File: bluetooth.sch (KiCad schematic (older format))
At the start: 53 parts, among them P100 CONN_2, P110 CONN_1, P111 CONN_1, P112 CONN_1, P113 CONN_1, P114 CONN_1, P115 CONN_1, P130 CONN_1, P131 CONN_1, Q1 MOSFET_N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

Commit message: Fix capacitor values for NCP1402
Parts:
- C12: value 10u -> 68u
- C15: value 68u -> 10u
- U3: value NCP1402 -> NCP1402SN50
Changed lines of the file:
@@
 P 2700 4900
 F 0 "U3" H 2700 4700 60  0000 C CNN
-F 1 "NCP1402" H 2700 5100 60  0000 C CNN
+F 1 "NCP1402SN50" H 2700 5100 60  0000 C CNN
 F 2 "" H 2700 4900 60  0000 C CNN
 F 3 "" H 2700 4900 60  0000 C CNN
@@
 P 4350 4850
 F 0 "C15" H 4400 4950 40  0000 L CNN
-F 1 "68u" H 4400 4750 40  0000 L CNN
+F 1 "10u" H 4400 4750 40  0000 L CNN
 F 2 "" H 4450 4700 30  0000 C CNN
 F 3 "" H 4350 4850 300 0000 C CNN
@@
 P 1600 4850
 F 0 "C12" H 1650 4950 40  0000 L CNN
-F 1 "10u" H 1650 4750 40  0000 L CNN
+F 1 "68u" H 1650 4750 40  0000 L CNN
 F 2 "" H 1700 4700 30  0000 C CNN
 F 3 "" H 1600 4850 300 0000 C CNN

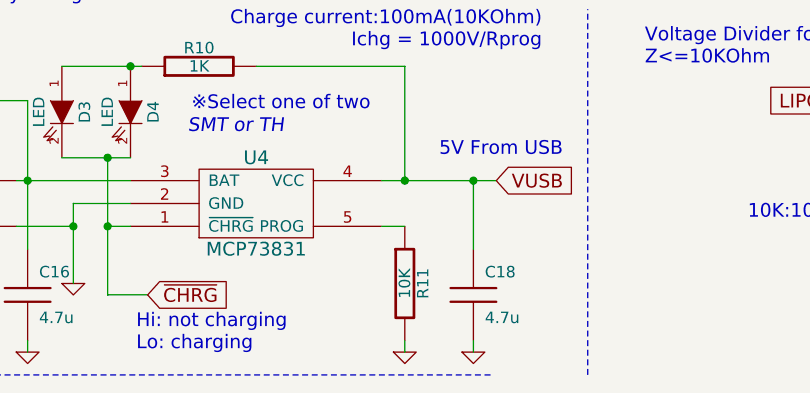
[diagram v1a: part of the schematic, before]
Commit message: Change value 10K to Rprog for charger resistor
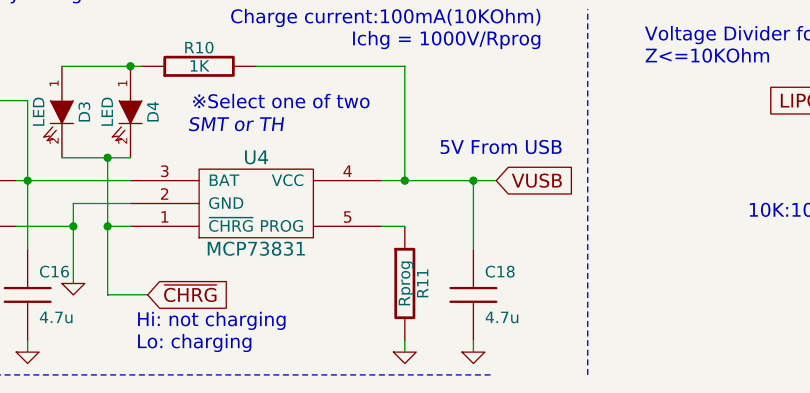
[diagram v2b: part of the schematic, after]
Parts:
- R11: value 10K -> Rprog
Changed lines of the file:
@@
 P 6200 7150
 F 0 "R11" V 6280 7150 50  0000 C CNN
-F 1 "10K" V 6200 7150 50  0000 C CNN
+F 1 "Rprog" V 6200 7150 50  0000 C CNN
 F 2 "" H 6200 7150 60  0000 C CNN
 F 3 "" H 6200 7150 60  0000 C CNN

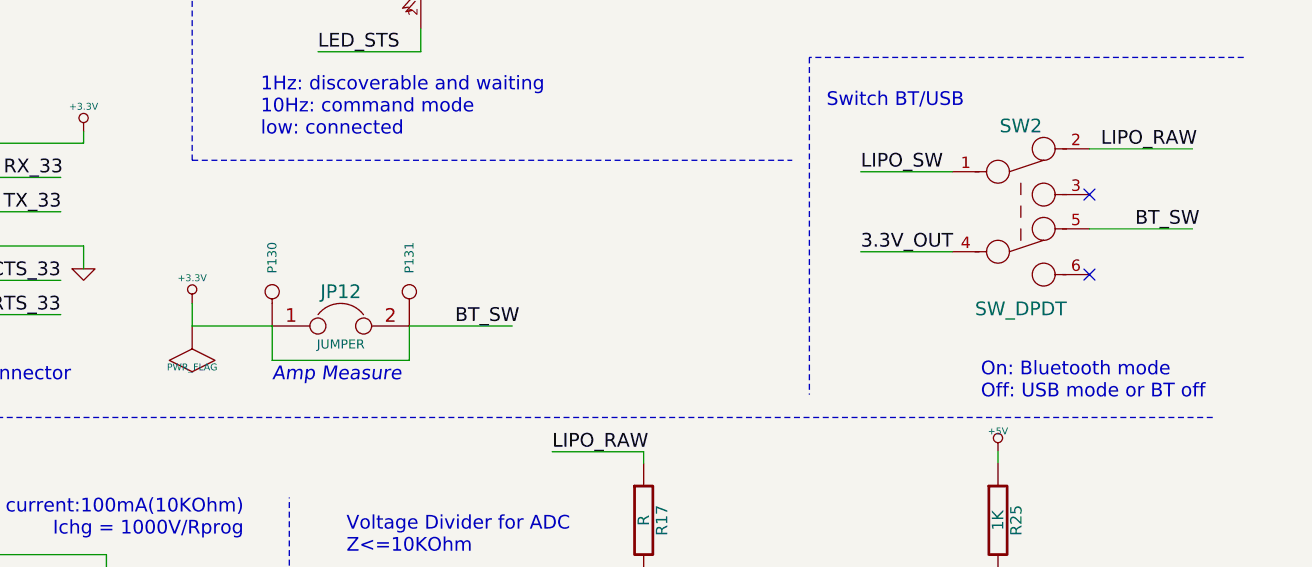
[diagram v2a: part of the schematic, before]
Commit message: Remove jumpers of 5V, 3.3V and HHKB amp measure
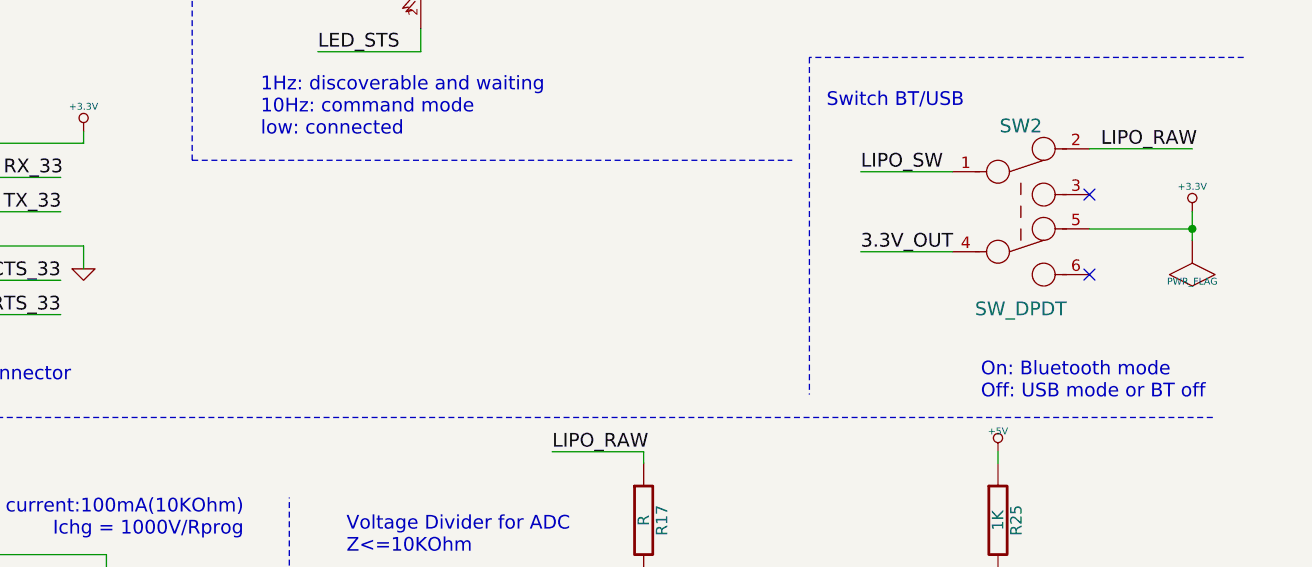
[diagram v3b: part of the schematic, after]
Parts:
- removed JP12: JUMPER, symbol JUMPER
- removed P130, P131: CONN_1, symbol CONN_1
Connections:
- net labels removed: BT_SW
- wire segments 142 -> 137
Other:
- note removed: "Amp Measure"
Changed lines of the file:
@@
 JST PH2
 $Comp
-L GND #PWR030
+L GND #PWR028
 U 1 1 51AFD4B7
 P 4750 7150
-F 0 "#PWR030" H 4750 7150 30  0001 C CNN
+F 0 "#PWR028" H 4750 7150 30  0001 C CNN
 F 1 "GND" H 4750 7080 30  0001 C CNN
 F 2 "" H 4750 7150 60  0000 C CNN
@@
 PSEL
 $Comp
-L GND #PWR031
+L GND #PWR029
 U 1 1 51B36189
 P 1600 5150
-F 0 "#PWR031" H 1600 5150 30  0001 C CNN
+F 0 "#PWR029" H 1600 5150 30  0001 C CNN
 F 1 "GND" H 1600 5080 30  0001 C CNN
 F 2 "" H 1600 5150 60  0000 C CNN
@@
 $EndComp
 $Comp
-L GND #PWR032
+L GND #PWR030
 U 1 1 51B36198
 P 4350 5150
-F 0 "#PWR032" H 4350 5150 30  0001 C CNN
+F 0 "#PWR030" H 4350 5150 30  0001 C CNN
 F 1 "GND" H 4350 5080 30  0001 C CNN
 F 2 "" H 4350 5150 60  0000 C CNN
@@
 $EndComp
 $Comp
-L GND #PWR033
+L GND #PWR031
 U 1 1 51B36208
 P 3400 5150
-F 0 "#PWR033" H 3400 5150 30  0001 C CNN
+F 0 "#PWR031" H 3400 5150 30  0001 C CNN
 F 1 "GND" H 3400 5080 30  0001 C CNN
 F 2 "" H 3400 5150 60  0000 C CNN
@@
 $EndComp
 $Comp
-L GND #PWR034
+L GND #PWR032
 U 1 1 51B4212D
 P 1250 3150
-F 0 "#PWR034" H 1250 3150 30  0001 C CNN
+F 0 "#PWR032" H 1250 3150 30  0001 C CNN
 F 1 "GND" H 1250 3080 30  0001 C CNN
 F 2 "" H 1250 3150 60  0000 C CNN
@@
 $EndComp
 $Comp
-L GND #PWR035
+L GND #PWR033
 U 1 1 51B4213C
 P 3300 3150
-F 0 "#PWR035" H 3300 3150 30  0001 C CNN
+F 0 "#PWR033" H 3300 3150 30  0001 C CNN
 F 1 "GND" H 3300 3080 30  0001 C CNN
 F 2 "" H 3300 3150 60  0000 C CNN
@@
 $EndComp
 $Comp
-L GND #PWR036
+L GND #PWR034
 U 1 1 51B421C0
 P 1650 3150
-F 0 "#PWR036" H 1650 3150 30  0001 C CNN
+F 0 "#PWR034" H 1650 3150 30  0001 C CNN
 F 1 "GND" H 1650 3080 30  0001 C CNN
 F 2 "" H 1650 3150 60  0000 C CNN
@@
 $EndComp
 $Comp
-L GND #PWR037
+L GND #PWR035
 U 1 1 51B42259
 P 3000 3350
-F 0 "#PWR037" H 3000 3350 30  0001 C CNN
+F 0 "#PWR035" H 3000 3350 30  0001 C CNN
 F 1 "GND" H 3000 3280 30  0001 C CNN
 F 2 "" H 3000 3350 60  0000 C CNN
@@
 $EndComp
 $Comp
-L GND #PWR038
+L GND #PWR036
 U 1 1 51B4294A
 P 4650 2050
-F 0 "#PWR038" H 4650 2050 30  0001 C CNN
+F 0 "#PWR036" H 4650 2050 30  0001 C CNN
 F 1 "GND" H 4650 1980 30  0001 C CNN
 F 2 "" H 4650 2050 60  0000 C CNN
@@
 $EndComp
 $Comp
-L +5V #PWR039
+L +5V #PWR037
 U 1 1 51B42AA7
 P 1850 1025
-F 0 "#PWR039" H 1850 1115 20  0001 C CNN
+F 0 "#PWR037" H 1850 1115 20  0001 C CNN
 F 1 "+5V" H 1850 1115 30  0000 C CNN
 F 2 "" H 1850 1025 60  0000 C CNN
@@
 $EndComp
 $Comp
-L +3.3V #PWR040
+L +3.3V #PWR038
 U 1 1 51B42AB6
 P 950 1025
-F 0 "#PWR040" H 950 985 30  0001 C CNN
+F 0 "#PWR038" H 950 985 30  0001 C CNN
 F 1 "+3.3V" H 950 1135 30  0000 C CNN
 F 2 "" H 950 1025 60  0000 C CNN
@@
 $EndComp
 $Comp
-L GND #PWR041
+L GND #PWR039
 U 1 1 51B44001
 P 6200 7450
-F 0 "#PWR041" H 6200 7450 30  0001 C CNN
+F 0 "#PWR039" H 6200 7450 30  0001 C CNN
 F 1 "GND" H 6200 7380 30  0001 C CNN
 F 2 "" H 6200 7450 60  0000 C CNN
@@
 BT UART connector
 $Comp
-L +3.3V #PWR042
+L +3.3V #PWR040
 U 1 1 51B8A63B
 P 6100 4350
-F 0 "#PWR042" H 6100 4310 30  0001 C CNN
+F 0 "#PWR040" H 6100 4310 30  0001 C CNN
 F 1 "+3.3V" H 6100 4460 30  0000 C CNN
 F 2 "" H 6100 4350 60  0000 C CNN
@@
 $EndComp
 $Comp
-L GND #PWR043
+L GND #PWR041
 U 1 1 51B8A64A
 P 6100 4950
-F 0 "#PWR043" H 6100 4950 30  0001 C CNN
+F 0 "#PWR041" H 6100 4950 30  0001 C CNN
 F 1 "GND" H 6100 4880 30  0001 C CNN
 F 2 "" H 6100 4950 60  0000 C CNN
@@
 $EndComp
 $Comp
-L GND #PWR044
+L GND #PWR042
 U 1 1 51B8BF6B
 P 6500 7450
-F 0 "#PWR044" H 6500 7450 30  0001 C CNN
+F 0 "#PWR042" H 6500 7450 30  0001 C CNN
 F 1 "GND" H 6500 7380 30  0001 C CNN
 F 2 "" H 6500 7450 60  0000 C CNN
@@
 $EndComp
 $Comp
-L CONN_1 P130
-U 1 1 51BB5CD5
-P 6925 5050
-F 0 "P130" H 7005 5050 40  0000 L CNN
-F 1 "CONN_1" H 6925 5105 30  0001 C CNN
-F 2 "" H 6925 5050 60  0000 C CNN
-F 3 "" H 6925 5050 60  0000 C CNN
-	1    6925 5050
-	0    -1   -1   0
-$EndComp
-$Comp
-L CONN_1 P131
-U 1 1 51BB5CE4
-P 7525 5050
-F 0 "P131" H 7605 5050 40  0000 L CNN
-F 1 "CONN_1" H 7525 5105 30  0001 C CNN
-F 2 "" H 7525 5050 60  0000 C CNN
-F 3 "" H 7525 5050 60  0000 C CNN
-	1    7525 5050
-	0    -1   -1   0
-$EndComp
-$Comp
-L JUMPER JP12
-U 1 1 51BB5CF3
-P 7225 5200
-F 0 "JP12" H 7225 5350 60  0000 C CNN
-F 1 "JUMPER" H 7225 5120 40  0000 C CNN
-F 2 "" H 7225 5200 60  0000 C CNN
-F 3 "" H 7225 5200 60  0000 C CNN
-	1    7225 5200
-	1    0    0    -1
-$EndComp
-Text Notes 6925 5450 0    60   Italic 0
-Amp Measure
-$Comp
 L LED D5
 U 1 1 51BC0B79
@@
 $EndComp
 $Comp
-L GND #PWR045
+L GND #PWR043
 U 1 1 51BE968F
 P 8550 6950
-F 0 "#PWR045" H 8550 6950 30  0001 C CNN
+F 0 "#PWR043" H 8550 6950 30  0001 C CNN
 F 1 "GND" H 8550 6880 30  0001 C CNN
 F 2 "" H 8550 6950 60  0000 C CNN
@@
 $EndComp
 $Comp
-L GND #PWR046
+L GND #PWR044
 U 1 1 52B7B3EE
 P 9875 3325
-F 0 "#PWR046" H 9875 3325 30  0001 C CNN
+F 0 "#PWR044" H 9875 3325 30  0001 C CNN
 F 1 "GND" H 9875 3255 30  0001 C CNN
 F 2 "" H 9875 3325 60  0000 C CNN
@@
 FACTORY_RESET
 $Comp
-L +3.3V #PWR047
+L +3.3V #PWR045
 U 1 1 52B7F387
 P 7600 750
-F 0 "#PWR047" H 7600 710 30  0001 C CNN
+F 0 "#PWR045" H 7600 710 30  0001 C CNN
 F 1 "+3.3V" H 7600 860 30  0000 C CNN
 F 2 "" H 7600 750 60  0000 C CNN
@@
 F.RST is not implemented,\nbe shorted with tweezer.\nON-OFF-ON-OFF-ON\nto restore factory default.\nPower on with turning ON.
 $Comp
-L +3.3V #PWR048
+L +3.3V #PWR046
 U 1 1 52B7F708
 P 7575 2850
-F 0 "#PWR048" H 7575 2810 30  0001 C CNN
+F 0 "#PWR046" H 7575 2810 30  0001 C CNN
 F 1 "+3.3V" H 7575 2960 30  0000 C CNN
 F 2 "" H 7575 2850 60  0000 C CNN
@@
 $EndComp
 $Comp
-L +5V #PWR049
+L +5V #PWR047
 U 1 1 52B840DE
 P 3775 1025
-F 0 "#PWR049" H 3775 1115 20  0001 C CNN
+F 0 "#PWR047" H 3775 1115 20  0001 C CNN
 F 1 "+5V" H 3775 1115 30  0000 C CNN
 F 2 "" H 3775 1025 60  0000 C CNN
@@
 $EndComp
 $Comp
-L +3.3V #PWR050
+L +3.3V #PWR048
 U 1 1 52B840E4
 P 2875 1025
-F 0 "#PWR050" H 2875 985 30  0001 C CNN
+F 0 "#PWR048" H 2875 985 30  0001 C CNN
 F 1 "+3.3V" H 2875 1135 30  0000 C CNN
 F 2 "" H 2875 1025 60  0000 C CNN
@@
 PSEL
 $Comp
-L GND #PWR051
+L GND #PWR049
 U 1 1 5310D0A7
 P 2650 7450
-F 0 "#PWR051" H 2650 7450 30  0001 C CNN
+F 0 "#PWR049" H 2650 7450 30  0001 C CNN
 F 1 "GND" H 2650 7380 30  0001 C CNN
 F 2 "" H 2650 7450 60  0000 C CNN
@@
 $EndComp
 $Comp
-L +5V #PWR052
+L +5V #PWR050
 U 1 1 5310EAB1
 P 1400 4300
-F 0 "#PWR052" H 1400 4390 20  0001 C CNN
+F 0 "#PWR050" H 1400 4390 20  0001 C CNN
 F 1 "+5V" H 1400 4390 30  0000 C CNN
 F 2 "" H 1400 4300 60  0000 C CNN
@@
 $EndComp
 $Comp
-L +5V #PWR053
+L +5V #PWR051
 U 1 1 5310EB6D
 P 950 2550
-F 0 "#PWR053" H 950 2640 20  0001 C CNN
+F 0 "#PWR051" H 950 2640 20  0001 C CNN
 F 1 "+5V" H 950 2640 30  0000 C CNN
 F 2 "" H 950 2550 60  0000 C CNN
@@
 LIPO_RAW
 $Comp
-L +3.3V #PWR054
+L +3.3V #PWR052
 U 1 1 5315633E
-P 6575 5100
-F 0 "#PWR054" H 6575 5060 30  0001 C CNN
-F 1 "+3.3V" H 6575 5210 30  0000 C CNN
-F 2 "" H 6575 5100 60  0000 C CNN
-F 3 "" H 6575 5100 60  0000 C CNN
-	1    6575 5100
+P 10950 4700
+F 0 "#PWR052" H 10950 4660 30  0001 C CNN
+F 1 "+3.3V" H 10950 4810 30  0000 C CNN
+F 2 "" H 10950 4700 60  0000 C CNN
+F 3 "" H 10950 4700 60  0000 C CNN
+	1    10950 4700
 	1    0    0    -1
 $EndComp
@@
 Text Label 3950 6350 0    60   ~ 0
 LIPO_RAW
-Text Label 10700 4775 0    60   ~ 0
-BT_SW
-$Comp
-L +3.3V #PWR055
+$Comp
+L +3.3V #PWR053
 U 1 1 5316AB09
 P 8325 2225
-F 0 "#PWR055" H 8325 2185 30  0001 C CNN
+F 0 "#PWR053" H 8325 2185 30  0001 C CNN
 F 1 "+3.3V" H 8325 2335 30  0000 C CNN
 F 2 "" H 8325 2225 60  0000 C CNN
@@
 $EndComp
 $Comp
-L GND #PWR056
+L GND #PWR054
 U 1 1 53177DE3
 P 5250 2050
-F 0 "#PWR056" H 5250 2050 30  0001 C CNN
+F 0 "#PWR054" H 5250 2050 30  0001 C CNN
 F 1 "GND" H 5250 1980 30  0001 C CNN
 F 2 "" H 5250 2050 60  0000 C CNN
@@
 $EndComp
 $Comp
-L +5V #PWR057
+L +5V #PWR055
 U 1 1 531B3A32
 P 10100 5750
-F 0 "#PWR057" H 10100 5840 20  0001 C CNN
+F 0 "#PWR055" H 10100 5840 20  0001 C CNN
 F 1 "+5V" H 10100 5840 30  0000 C CNN
 F 2 "" H 10100 5750 60  0000 C CNN
@@
 NoConn ~ 10500 4975
 NoConn ~ 10500 4625
-Text Label 7725 5200 0    60   ~ 0
-BT_SW
 Text Label 3500 2650 0    60   ~ 0
 3.3V_OUT
 Text Label 9500 4875 0    60   ~ 0
 3.3V_OUT
-$Comp
-L PWR_FLAG #FLG058
-U 1 1 531F4430
-P 6575 5200
-F 0 "#FLG058" H 6575 5295 30  0001 C CNN
-F 1 "PWR_FLAG" H 6575 5380 30  0000 C CNN
-F 2 "" H 6575 5200 60  0000 C CNN
-F 3 "" H 6575 5200 60  0000 C CNN
-	1    6575 5200
-	-1   0    0    1
-$EndComp
 Text Notes 1800 4275 0    60   ~ 0
 MBR0520LT1 20V 1A\nRMB160M-30 30V 1A*
@@
 $EndComp
 $Comp
-L GND #PWR059
+L GND #PWR056
 U 1 1 53B572EF
 P 4550 7450
-F 0 "#PWR059" H 4550 7450 30  0001 C CNN
+F 0 "#PWR056" H 4550 7450 30  0001 C CNN
 F 1 "GND" H 4550 7380 30  0001 C CNN
 F 2 "" H 4550 7450 60  0000 C CNN
@@
 $EndComp
 $Comp
-L GND #PWR060
+L GND #PWR057
 U 1 1 53C70129
 P 5900 2050
-F 0 "#PWR060" H 5900 2050 30  0001 C CNN
+F 0 "#PWR057" H 5900 2050 30  0001 C CNN
 F 1 "GND" H 5900 1980 30  0001 C CNN
 F 2 "" H 5900 2050 60  0000 C CNN
@@
 	8325 2225 8325 2325
 Wire Wire Line
-	6575 5200 6925 5200
-Wire Wire Line
-	6575 5100 6575 5200
-Wire Wire Line
-	7525 5200 7975 5200
-Wire Wire Line
-	7525 5350 7525 5200
-Wire Wire Line
 	950  2550 950  2650
 Wire Wire Line
@@
 Wire Wire Line
 	9900 4525 9500 4525
-Wire Wire Line
-	10500 4775 10950 4775
 Wire Wire Line
 	10500 4425 10950 4425
@@
 	4900 6600 4900 7200
 Connection ~ 4900 6600
-Wire Wire Line
-	6925 5200 6925 5350
-Wire Wire Line
-	6925 5350 7525 5350
 Wire Wire Line
 	8550 6300 8550 6400
@@
 NoConn ~ 9025 1425
 NoConn ~ 9025 1825
+Wire Wire Line
+	10500 4775 10950 4775
+Wire Wire Line
+	10950 4700 10950 4825
+$Comp
+L PWR_FLAG #FLG058
+U 1 1 531F4430
+P 10950 4825
+F 0 "#FLG058" H 10950 4920 30  0001 C CNN
+F 1 "PWR_FLAG" H 10950 5005 30  0000 C CNN
+F 2 "" H 10950 4825 60  0000 C CNN
+F 3 "" H 10950 4825 60  0000 C CNN
+	1    10950 4825
+	-1   0    0    1
+$EndComp
+Connection ~ 10950 4775
 $EndSCHEMATC
